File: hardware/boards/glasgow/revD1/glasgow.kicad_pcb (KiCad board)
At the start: 6 copper layers, 95 x 55 mm, 775 parts, among them J1 USB-C, J10 P1, J11 CLK_EXT, J12 FPGA_TP, J2 SWD, J3 COM, J4 SYNC, J5 JTAG, J6 LVDS, J7 P1, J8 P1, J9 P1, Q1 AO3401, Q2 AO3400, SW1 RST, U1 BL24C256A-SFRC, U10 74AXP1T45, U11 XccelaOPI, U12 XccelaOPI, U13 TLV62569PDRL, U14 TLV62569PDRL, U15 TLV61070ADBV, U16 APX811-40UG-7, U17 TLV77525DRL, U18 TLV62569PDRL, U19 TPS7A2033, U2 CY7C68013A-56LTX, U20 TPS22917DBV, U21 DAC43204, U22 LMR54406, U23 SY7208CABC, U24 TCA6416APW, U25 TCA6416APW, U26 74AXP1T45, U27 74AXP1T45, U28 TPS629203, U29 74AXP1T45, U3 TMP112xxDRL, U30 74AXP1T45, U31 74AXP1T45, U32 74AXP1T45, U33 NCP456R, U34 INA233, U35 74AXP1T45, U36 74AXP1T45, U37 TLV6001DCK, U38 74AXP1T45, U39 74AXP1T45, U4 FUSB302B01MPX, U40 TPS629203, U41 74AXP1T45, U42 74AXP1T45, U43 74AXP1T45, U44 74AXP1T45, U45 NCP456R, U46 INA233, U47 74AXP1T45, U48 74AXP1T45, U49 TLV6001DCK, U5 TPS259472ARPW, U50 74AXP1T45, U51 74AXP1T45, U52 TPS629203, U53 74AXP1T45, U54 74AXP1T45, U55 74AXP1T45, U56 74AXP1T45, U57 NCP456R, U58 INA233, U59 74AXP1T45, U6 STM32G031G6Ux, U60 74AXP1T45, U61 TLV6001DCK, U62 74AXP1T45, U63 74AXP1T45, U64 TPS629203, U65 74AXP1T45, U66 74AXP1T45, U67 74AXP1T45, U68 74AXP1T45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

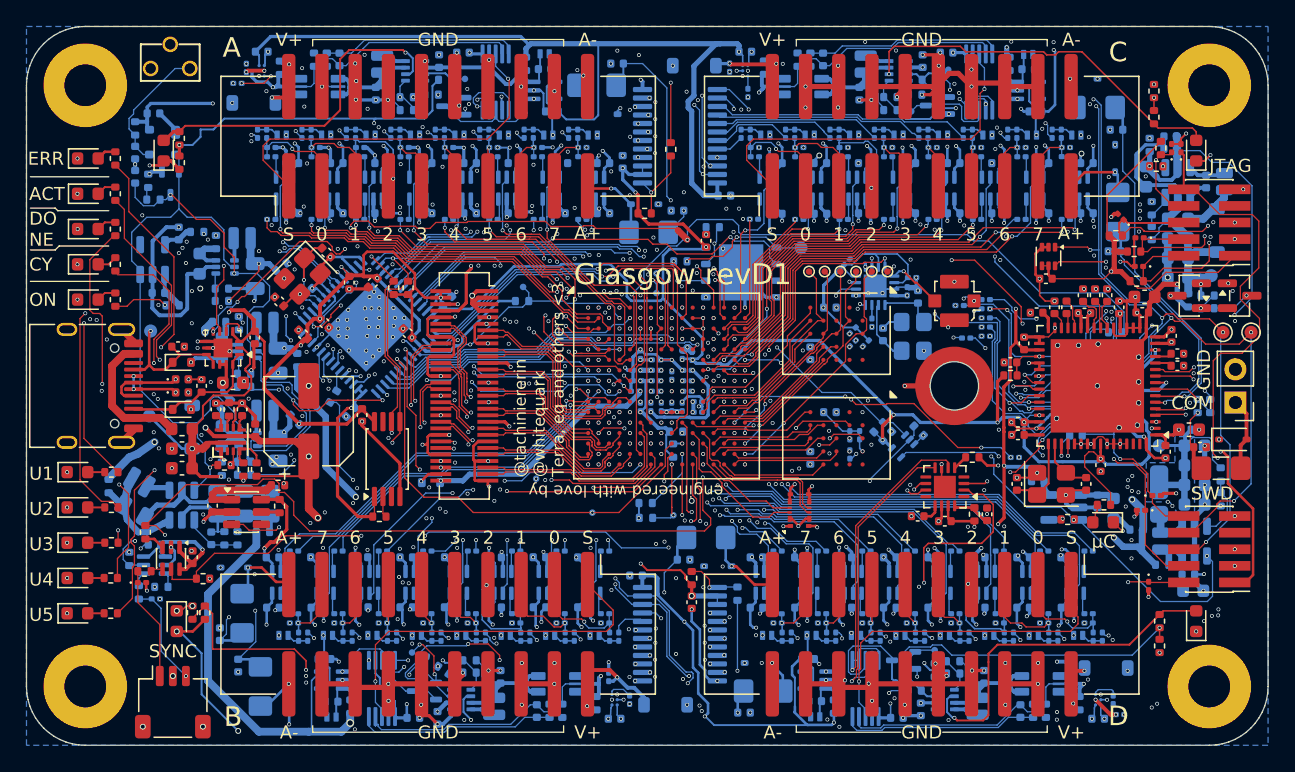
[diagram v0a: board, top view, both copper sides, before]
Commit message: fix some more silk issues
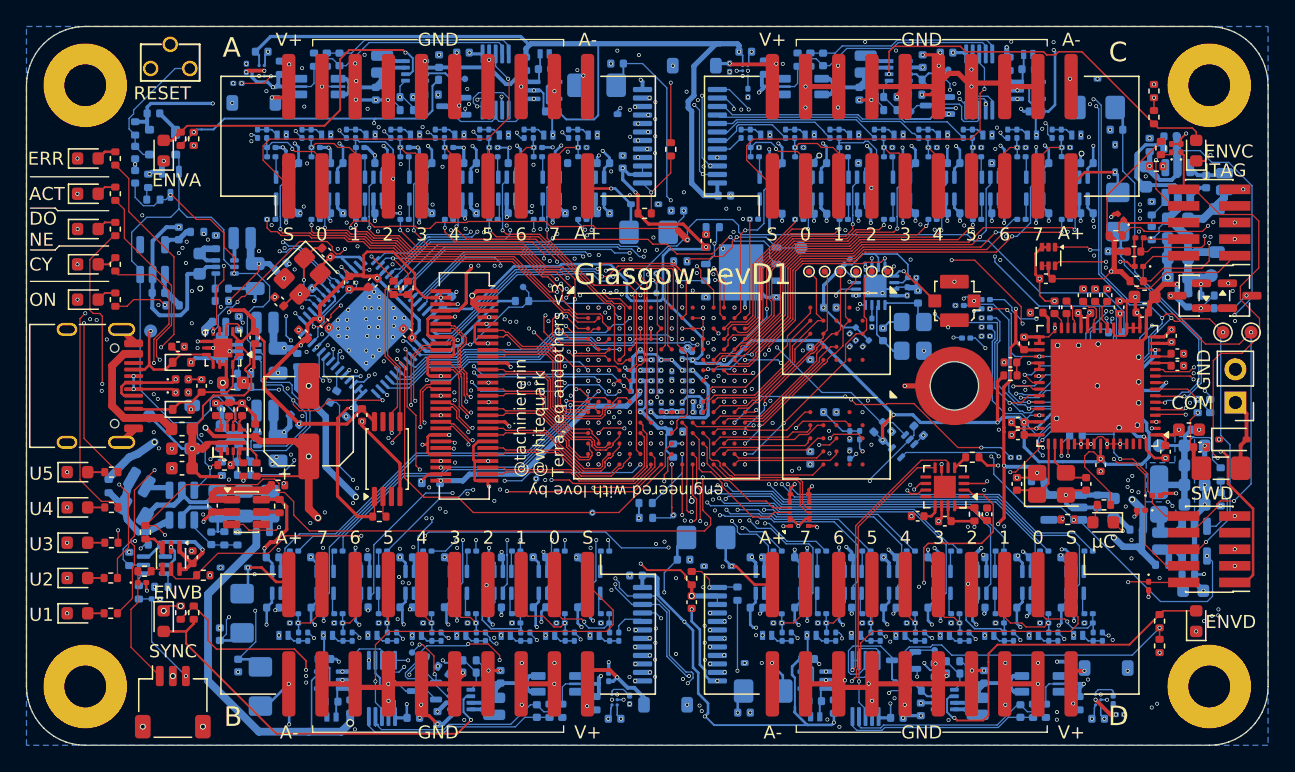
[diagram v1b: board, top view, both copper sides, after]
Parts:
- moved R10 2.13 mm to (128.1, 89.3)
- moved D60 1.00 mm to (125.8, 126.2)
- moved R11 0.90 mm to (127.1, 125.5)
- moved R126 0.85 mm to (128.1, 125.5)
- moved R47 0.26 mm to (128.8, 122.7)
- moved R84 0.11 mm to (127.1, 89.3)
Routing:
- net GND: track 431.7 -> 429.1 mm, vias 679 -> 680
- net /ENVA: track 46.2 -> 45.0 mm
- net /IO Banks/Bank B/PG: track 33.1 -> 32.1 mm, vias 3 -> 1
- net Net-(U10-DIR): track 60.5 -> 60.0 mm
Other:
- board text added: "ENVA"
- board text added: "ENVB"
- board text added: "ENVC"
- board text added: "ENVD"
- board text added: "RESET"
